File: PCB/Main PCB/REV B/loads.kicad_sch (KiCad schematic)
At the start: 9 parts, among them J10 Ignitor, J11 Auger, J12 FAN, U8 AQH3223A

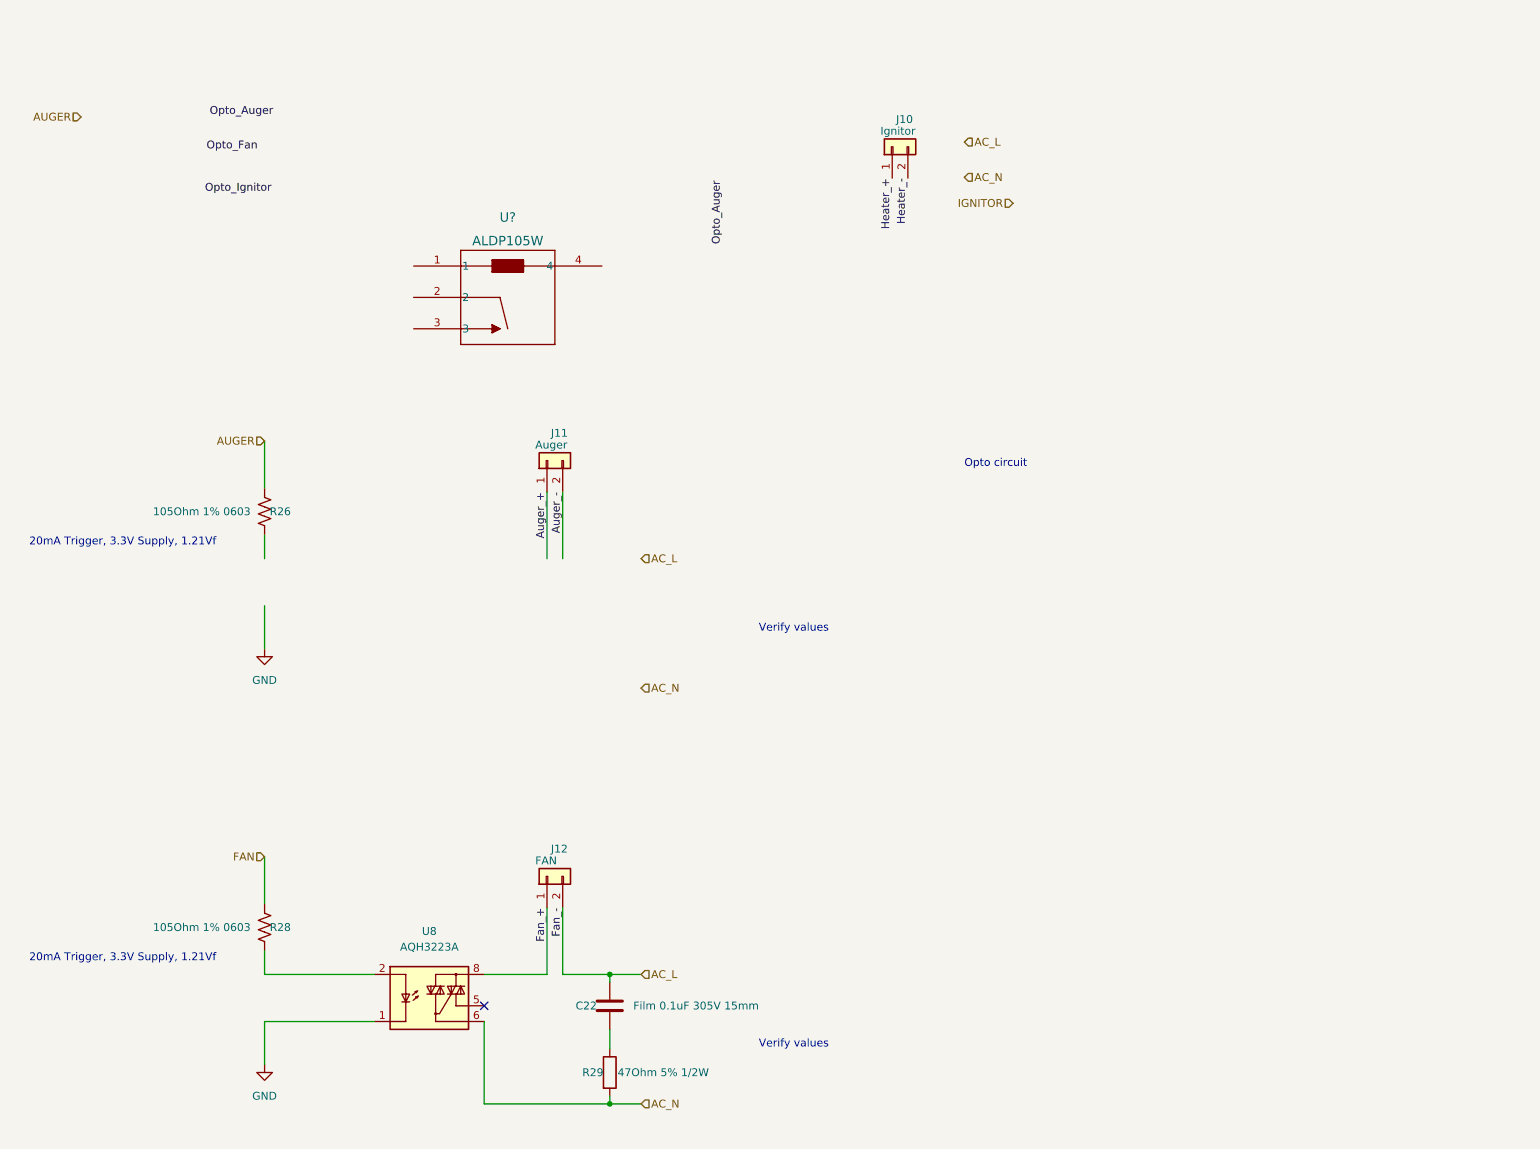
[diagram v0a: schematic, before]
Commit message: PCB schematic updates, Modified and fixed all power sheets
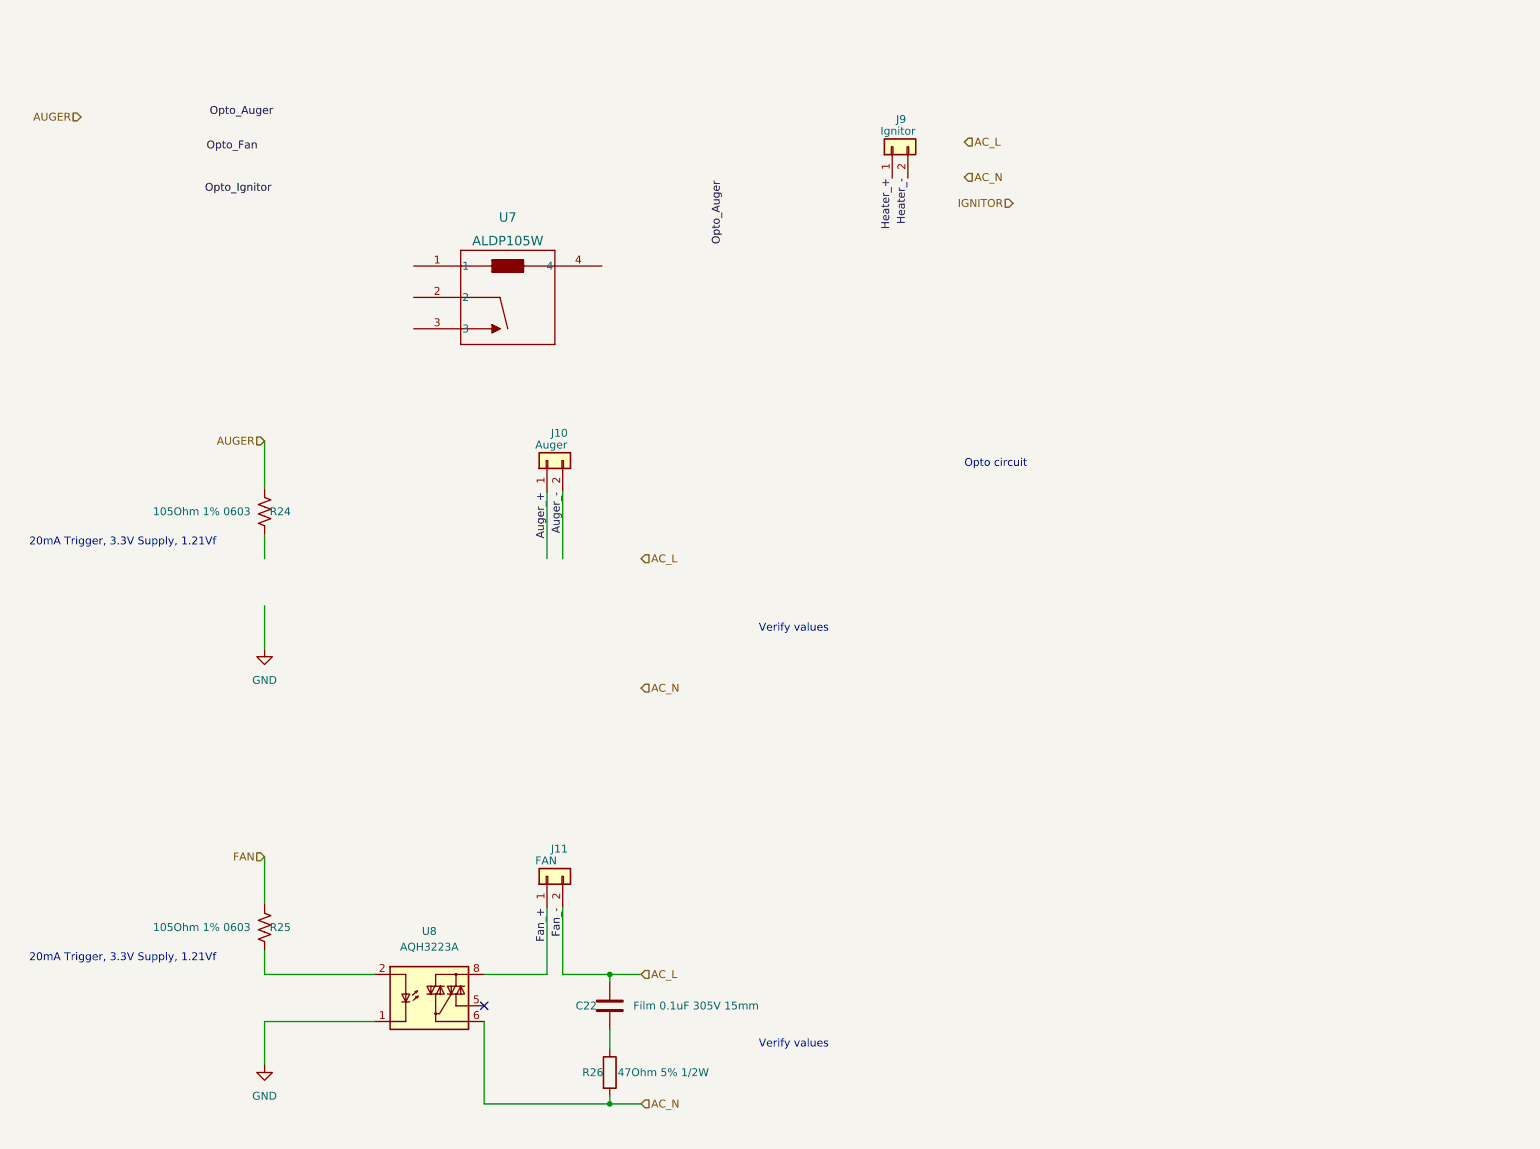
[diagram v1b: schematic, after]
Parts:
- gave numbers to parts that had none: 1
- renumbered J11 to J10, J12 to J11, J10 to J9, R26 to R24, R28 to R25, R29 to R26
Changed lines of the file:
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@@
   (symbol (lib_id "Connector_Generic:Conn_01x02") (at 120.65 153.67 90) (unit 1)
     (in_bom yes) (on_board yes)
-    (property "Reference" "J12" (id 0) (at 121.285 149.225 90)
+    (property "Reference" "J11" (id 0) (at 121.285 149.225 90)
       (effects (font (size 1.27 1.27)) (justify right))
     )
@@
   (symbol (lib_id "ALDP105W:ALDP105W") (at 99.06 54.864 0) (unit 1)
     (in_bom yes) (on_board yes) (fields_autoplaced)
-    (property "Reference" "U?" (id 0) (at 114.3 46.99 0)
+    (property "Reference" "U7" (id 0) (at 114.3 46.99 0)
       (effects (font (size 1.524 1.524)))
     )
@@
   (symbol (lib_id "power:GND") (at 74.93 116.84 0) (mirror y) (unit 1)
     (in_bom yes) (on_board yes)
-    (property "Reference" "#PWR072" (id 0) (at 74.93 123.19 0)
+    (property "Reference" "#PWR069" (id 0) (at 74.93 123.19 0)
       (effects (font (size 1.27 1.27)) hide)
     )
@@
   (symbol (lib_id "Device:R_US") (at 74.93 161.925 0) (unit 1)
     (in_bom yes) (on_board yes)
-    (property "Reference" "R28" (id 0) (at 77.47 161.925 0))
+    (property "Reference" "R25" (id 0) (at 77.47 161.925 0))
     (property "Value" "105Ohm 1% 0603" (id 1) (at 64.77 161.925 0))
     (property "Footprint" "Resistor_SMD:R_0603_1608Metric" (id 2) (at 75.946 162.179 90)
@@
   (symbol (lib_id "power:GND") (at 74.93 184.15 0) (mirror y) (unit 1)
     (in_bom yes) (on_board yes)
-    (property "Reference" "#PWR073" (id 0) (at 74.93 190.5 0)
+    (property "Reference" "#PWR070" (id 0) (at 74.93 190.5 0)
       (effects (font (size 1.27 1.27)) hide)
     )
@@
   (symbol (lib_id "Device:R") (at 130.81 185.42 0) (unit 1)
     (in_bom yes) (on_board yes)
-    (property "Reference" "R29" (id 0) (at 126.365 185.42 0)
+    (property "Reference" "R26" (id 0) (at 126.365 185.42 0)
       (effects (font (size 1.27 1.27)) (justify left))
     )
@@
   (symbol (lib_id "Device:R_US") (at 74.93 94.615 0) (unit 1)
     (in_bom yes) (on_board yes)
-    (property "Reference" "R26" (id 0) (at 77.47 94.615 0))
+    (property "Reference" "R24" (id 0) (at 77.47 94.615 0))
     (property "Value" "105Ohm 1% 0603" (id 1) (at 64.77 94.615 0))
     (property "Footprint" "Resistor_SMD:R_0603_1608Metric" (id 2) (at 75.946 94.869 90)
@@
   (symbol (lib_id "Connector_Generic:Conn_01x02") (at 176.53 35.56 90) (unit 1)
     (in_bom yes) (on_board yes)
-    (property "Reference" "J10" (id 0) (at 177.165 31.115 90)
+    (property "Reference" "J9" (id 0) (at 177.165 31.115 90)
       (effects (font (size 1.27 1.27)) (justify right))
     )
@@
   (symbol (lib_id "Connector_Generic:Conn_01x02") (at 120.65 86.36 90) (unit 1)
     (in_bom yes) (on_board yes)
-    (property "Reference" "J11" (id 0) (at 121.285 81.915 90)
-      (effects (font (size 1.27 1.27)) (justify right))
-    )
+    (property "Reference" "J10" (id 0) (at 121.285 81.915 90)
+      (effects (font (size 1.27 1.27)) (justify right))
+    )

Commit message: PCB schematic updates, Added optoisolators for relay circuits
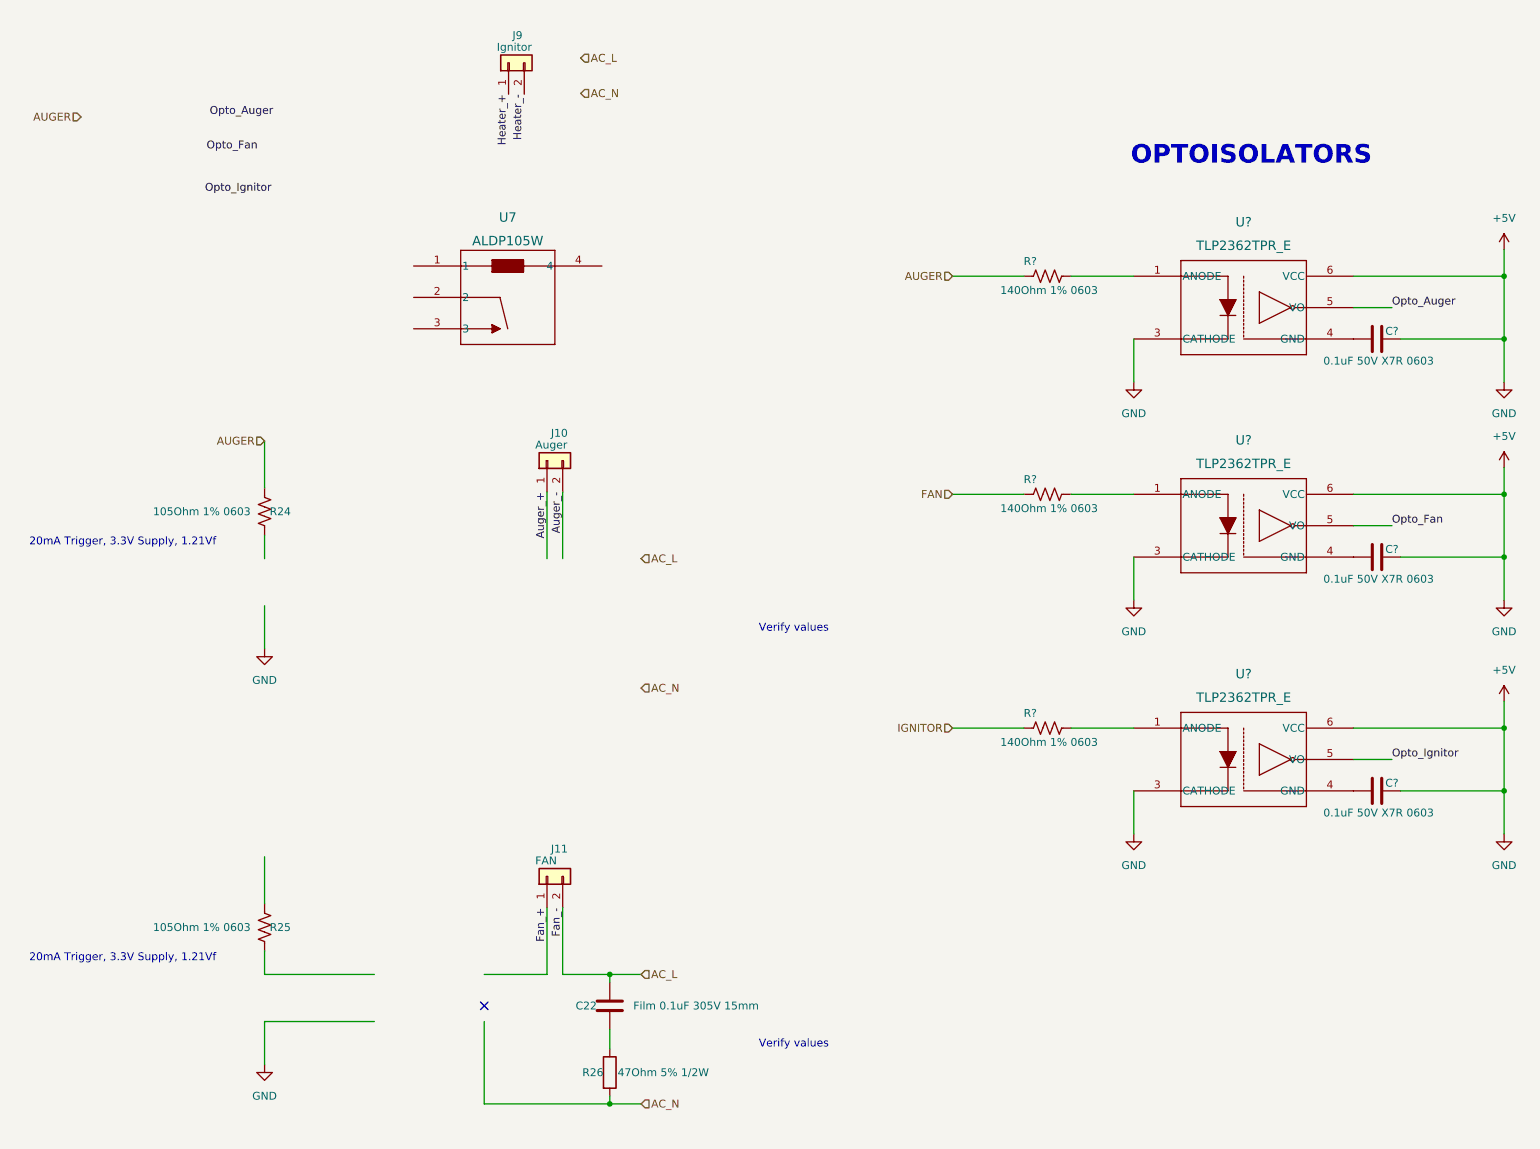
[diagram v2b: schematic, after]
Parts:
- removed U8: AQH3223A, Package_SO:SSO-7-8_6.4x9.78mm_P2.54mm, symbol Relay_SolidState:AQH3223A
- added C? (x3): 0.1uF 50V X7R 0603, Capacitor_SMD:C_0603_1608Metric, symbol Device:C
- added R? (x3): 140Ohm 1% 0603, Resistor_SMD:R_0603_1608Metric, symbol Device:R_US
- added U? (x3): TLP2362TPR_E, 11-4L1S_TOS, symbol TLP2362:TLP2362TPR_E
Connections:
- net AUGER: now also R?.1
- net FAN: now also R?.1; no longer R25.1
- net IGNITOR: now also R?.1
- net Opto_Auger: now also U?.5 (VO)
- net Opto_Fan: now also U?.5 (VO)
- net Opto_Ignitor: now also U?.5 (VO)
- new net: R?.2, U?.1 (ANODE) (x3)
- new net: C?.2, U?.4 (GND) (x3)
- new net +5V: C?.1, C?.1, C?.1, U?.3 (CATHODE), U?.3 (CATHODE), U?.3 (CATHODE), U?.6 (VCC), U?.6 (VCC), U?.6 (VCC)
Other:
- note added: "OPTOISOLATORS"
- note removed: "Opto circuit"
- moved on the sheet: J9

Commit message: PCB schematic updates, Find mosfet for relay on circuit
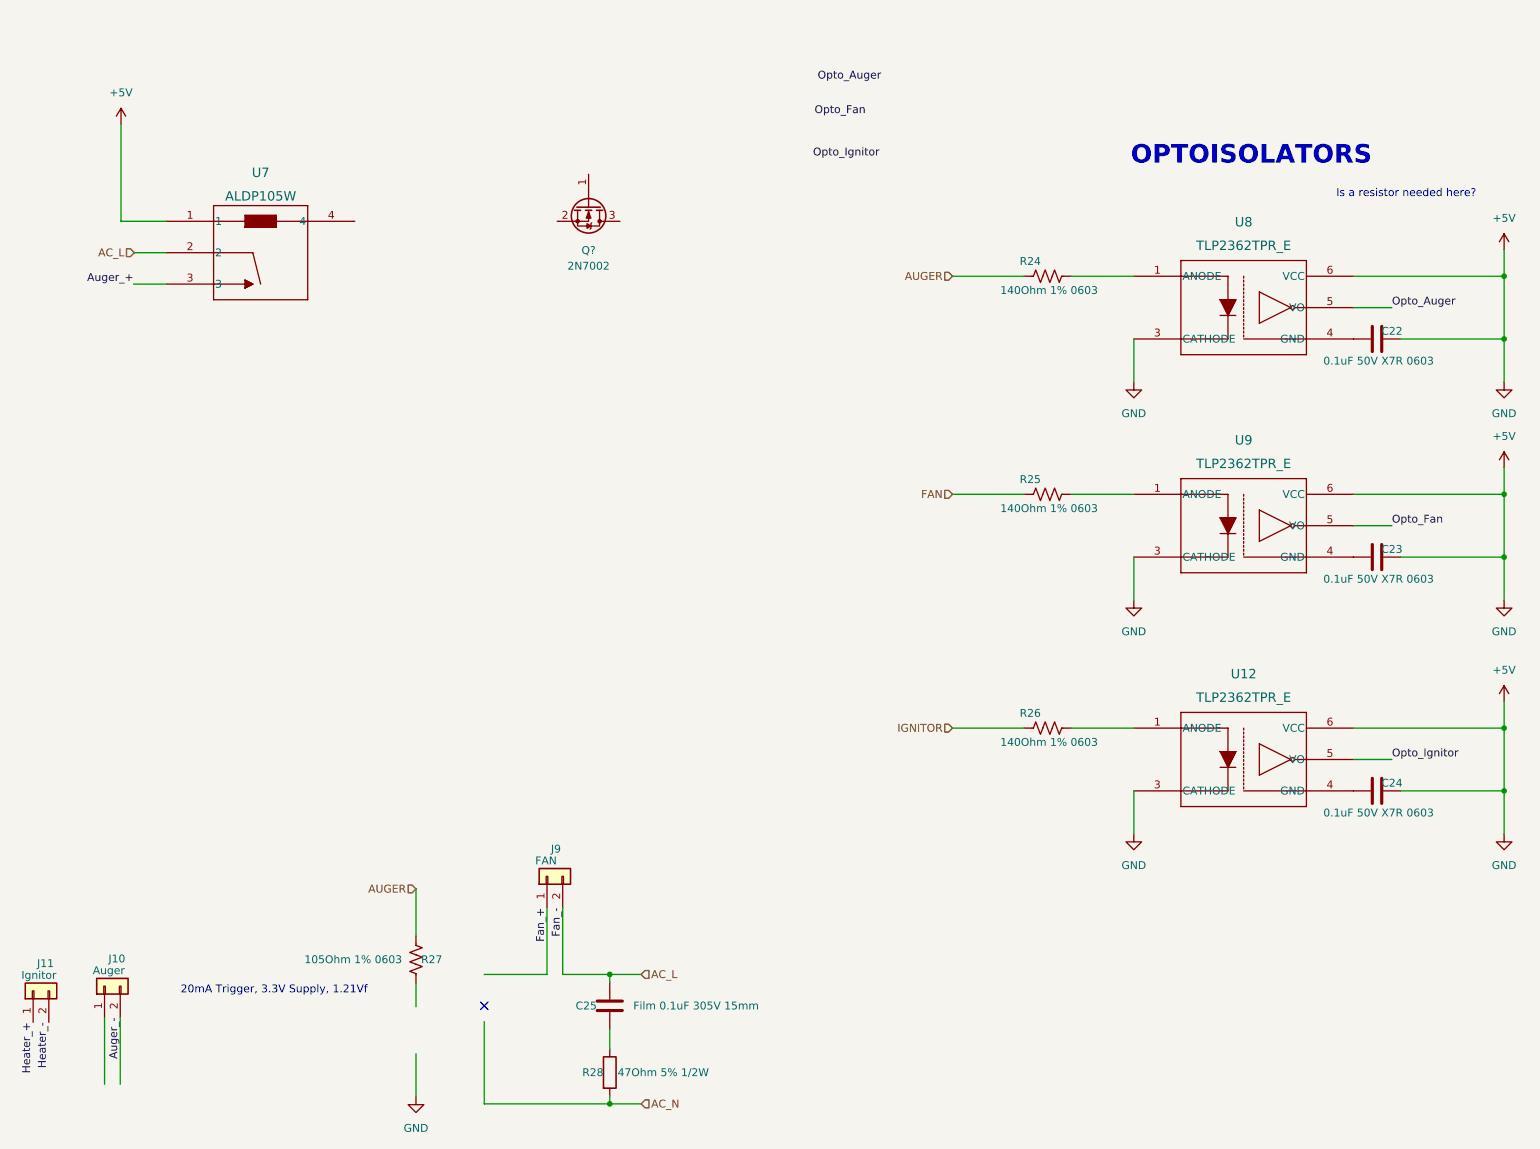
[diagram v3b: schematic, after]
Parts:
- removed R25: 105Ohm 1% 0603, Resistor_SMD:R_0603_1608Metric, symbol Device:R_US
- removed U? (x2): TLP2362TPR_E, 11-4L1S_TOS, symbol TLP2362:TLP2362TPR_E
- added Q?: 2N7002, Package_TO_SOT_SMD:SOT-23, symbol Transistor_FET:2N7002
- added U12, U9: TLP2362TPR_E, Customs Smoker:TLP2362, symbol TLP2362:TLP2362TPR_E
- U7: footprint PAN_ALD_PAN -> Customs Smoker:PAN_ALD_PAN; Manufacturer (none) -> Panasonic Electric Works; Manufacturer Part Number (none) -> ALDP105W; Vendor (none) -> Digikey; Vendor Part Number (none) -> 255-3586-ND
- U8: renamed from U?; footprint 11-4L1S_TOS -> Customs Smoker:TLP2362; Manufacturer (none) -> Toshiba Semiconductor and Storage; Manufacturer Part Number (none) -> TLP2362(TPR,E; Vendor (none) -> Digikey; Vendor Part Number (none) -> TLP2362(TPRECT-ND
- gave numbers to parts that had none: 6
- renumbered C22 to C25, J9 to J11, J11 to J9, R24 to R27, R26 to R28
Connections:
- net +5V: now also U7.1, U12.3 (CATHODE), U12.6 (VCC), U9.3 (CATHODE), U9.6 (VCC)
- net AC_L: now also U7.2
- net Auger_+: now also U7.3; no longer J10.1 (Pin_1)
- net Opto_Fan: now also U9.5 (VO)
- net Opto_Ignitor: now also U12.5 (VO)
- net at R26.2: now also U12.1 (ANODE)
- net at C24.2: now also U12.4 (GND)
- net at R25.2: now also U9.1 (ANODE)
- net at C23.2: now also U9.4 (GND)
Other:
- note added: "Is a resistor needed here?"
- note removed: "Verify values"
- moved on the sheet: J10, J11, R27, U7
